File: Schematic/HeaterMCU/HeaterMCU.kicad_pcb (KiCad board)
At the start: 2 copper layers, 100 x 35 mm, 58 parts, among them J301 To µTracer, J302 Firmware, J303 To PSU Board, Q301 BSS138, Q302 BSS138, SW301 RESET, U301 TPS54302, U302 ATMEGA328P-AU, U303 INA219AIDCNR, U304 Display_IPS_1.3_SPI, Y301 8MHz

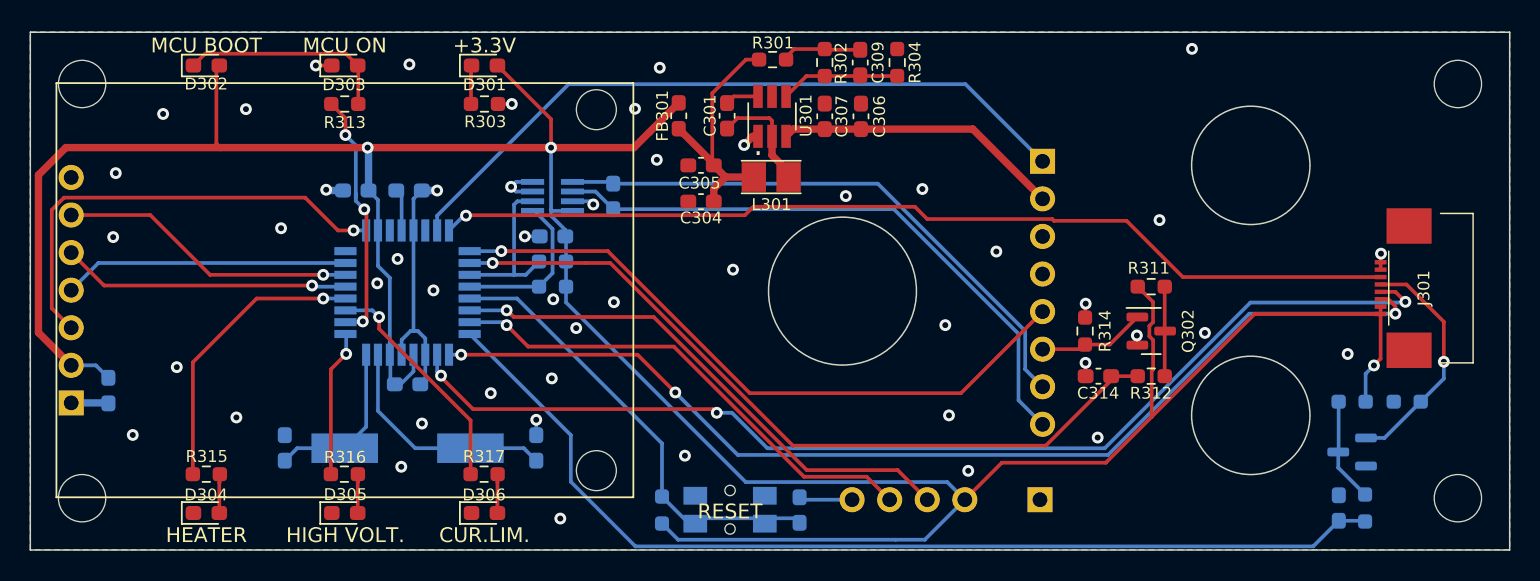
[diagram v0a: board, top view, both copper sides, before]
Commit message: Added output filter caps + spacing around mounting holes
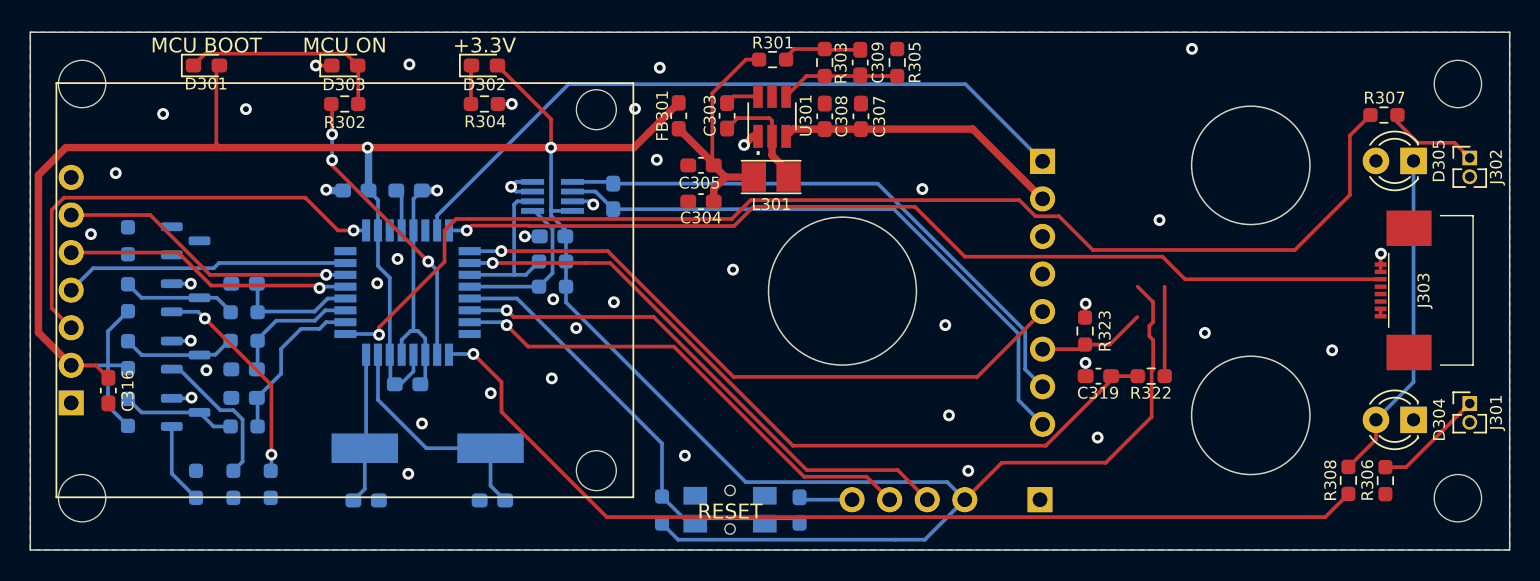
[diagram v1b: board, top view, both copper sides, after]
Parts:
- removed the D304 at (66.9, 77.5)
- added C313: 1µF, Capacitor_SMD:C_0603_1608Metric_Pad1.08x0.95mm_HandSolder, B.Cu at (69.5, 67.8)
- added C315: 1µF, Capacitor_SMD:C_0603_1608Metric_Pad1.08x0.95mm_HandSolder, B.Cu at (69.5, 62.0)
- added J301: Ext.LED, Connector_PinHeader_1.27mm:PinHeader_1x02_P1.27mm_Vertical, F.Cu at (152.3, 70.1)
- added J302: Ext.LED, Connector_PinHeader_1.27mm:PinHeader_1x02_P1.27mm_Vertical, F.Cu at (152.3, 53.5)
- added Q301: BSS138, Package_TO_SOT_SMD:SOT-23, B.Cu at (65.5, 66.8)
- added Q302: BSS138, Package_TO_SOT_SMD:SOT-23, B.Cu at (65.5, 63.0)
- added R312: 1MΩ, Resistor_SMD:R_0603_1608Metric_Pad0.98x0.95mm_HandSolder, B.Cu at (61.6, 66.8)
- added R313: 220Ω, Resistor_SMD:R_0603_1608Metric_Pad0.98x0.95mm_HandSolder, B.Cu at (69.5, 65.9)
- added R314: 100kΩ, Resistor_SMD:R_0603_1608Metric_Pad0.98x0.95mm_HandSolder, B.Cu at (68.7, 75.6)
- added R315: 1MΩ, Resistor_SMD:R_0603_1608Metric_Pad0.98x0.95mm_HandSolder, B.Cu at (61.6, 63.0)
- added R316: 220Ω, Resistor_SMD:R_0603_1608Metric_Pad0.98x0.95mm_HandSolder, B.Cu at (69.5, 63.9)
- added R317: 100kΩ, Resistor_SMD:R_0603_1608Metric_Pad0.98x0.95mm_HandSolder, B.Cu at (71.2, 75.6)
- C316: moved to F.Cu
- D304: renamed from D306; footprint LED_SMD:LED_0603_1608Metric_Pad1.05x0.95mm_HandSolder -> LED_THT:LED_D3.0mm
- D305: value "High Voltage" -> "Voltage limit"; footprint LED_SMD:LED_0603_1608Metric_Pad1.05x0.95mm_HandSolder -> LED_THT:LED_D3.0mm
- Q304: renamed from Q302; moved to B.Cu
- R306: renamed from R315; value 560Ω -> 330Ω
- R321: renamed from R311; moved to B.Cu
- moved R318 82.8 mm to (61.6, 70.7), turned to 90 degrees
- moved R320 82.1 mm to (66.2, 75.6), turned to 90 degrees
- moved R306 79.7 mm to (146.6, 75.3), turned to -90 degrees
- moved Q303 78.9 mm to (65.5, 70.7), turned to 0 degrees
- moved D305 76.1 mm to (148.5, 53.7), turned to 180 degrees
- moved R319 76.0 mm to (69.5, 71.7), turned to 180 degrees
- moved C318 74.4 mm to (69.5, 69.7), turned to 0 degrees
- moved R307 74.3 mm to (146.5, 50.6)
- moved R321 69.2 mm to (61.6, 59.1), turned to 90 degrees
- moved Q304 65.6 mm to (65.5, 59.1)
- moved D304 63.1 mm to (148.5, 71.2), turned to 180 degrees
- moved R308 58.4 mm to (144.1, 75.3), turned to -90 degrees
- moved C310 6.55 mm to (77.7, 76.7), turned to 0 degrees
- moved C306 4.62 mm to (86.2, 76.7), turned to 180 degrees
- moved Y301 1.36 mm to (81.9, 73.1)
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- renumbered C302 to C301, C303 to C302, C301 to C303, C308 to C306, C306 to C307, C307 to C308, C313 to C312, C315 to C314, C312 to C318, C314 to C319, D302 to D301, D301 to D302, J301 to J303, J302 to J304, J303 to J305, Q301 to Q303, R313 to R302, R302 to R303, R303 to R304, R304 to R305, R316 to R307, R317 to R308, R307 to R309, R308 to R310, R309 to R311, R305 to R318, R306 to R319, R310 to R320, R312 to R322, R314 to R323
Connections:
- net /FlagHeater renamed PULSE_HEATER
- net CUR_LIM renamed PULSE_CUR_LIM
- net FLAG_CUR_LIM_FILT renamed FLAG_CUR_LIM
- C318 pad 2: FLAG_HEATER_FILT -> FLAG_HEATER
- D304 pad 2: Net-(D306-Pad2) -> Net-(D304-Pad2)
- D305 pad 1: GNDPWR -> Net-(D304-Pad2)
- D305 pad 2: Net-(D305-Pad2) -> +3V3
- J303 pad 3: Spare2 -> PULSE_ANODE
- J303 pad 4: Spare1 -> PULSE_GRID
- R307 pad 1: Net-(D305-Pad2) -> Net-(J302-Pad1)
- R308 pad 1: Net-(D306-Pad2) -> Net-(D304-Pad2)
- R308 pad 2: LED_CURRENT_LIMIT -> LED_LIMIT_V_I
- R319 pad 1: FLAG_HEATER_FILT -> FLAG_HEATER
- U302 pad 1: Spare2 -> LED_LIMIT_V_I
- U302 pad 10: LED_MCU_STATUS -> FLAG_HEATER
- U302 pad 11: LED_CURRENT_LIMIT -> FLAG_ANODE
- U302 pad 12: LED_HEATER -> FLAG_GRID
- U302 pad 2: Spare1 -> LED_MCU_STATUS
- U302 pad 32: FLAG_HEATER_FILT -> LED_HEATER
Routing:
- net Spare1: track 74.9 -> 0.00 mm, vias 3 -> 0
- net LED_HIGH_VOLTAGE: track 9.62 -> 82.1 mm
- net Spare2: track 72.4 -> 0.00 mm, vias 3 -> 0
- net FLAG_HEATER_FILT: track 69.1 -> 0.00 mm
- net LED_LIMIT_V_I: track 0.00 -> 67.2 mm, vias 0 -> 1
- net Net-(D304-Pad2): track 0.00 -> 22.5 mm
- net LED_HEATER: track 19.4 -> 0.00 mm, vias 1 -> 0
- net LED_CURRENT_LIMIT: track 15.6 -> 0.00 mm, vias 1 -> 0
- net PULSE_GRID: track 0.00 -> 14.6 mm, vias 0 -> 2
- net +3V3: track 210.8 -> 198.9 mm, vias 3 -> 2
- net FLAG_HEATER: track 0.00 -> 11.0 mm
- net PULSE_HEATER: track 16.1 -> 5.50 mm, vias 1 -> 0
- net PULSE_ANODE: track 0.00 -> 9.93 mm
- net FLAG_ANODE: track 0.00 -> 8.66 mm
- net FLAG_GRID: track 0.00 -> 8.21 mm
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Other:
- board text added: "µTracer Heater MCU 22_43_0120F Bjørner Sandom"
- board text removed: "CUR.LIM."
- board text removed: "HEATER"
- board text removed: "HIGH VOLT."
- board text removed: "µTracer Heater MCU 22_43_0120E Bjørner Sandom"

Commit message: New status LED layout
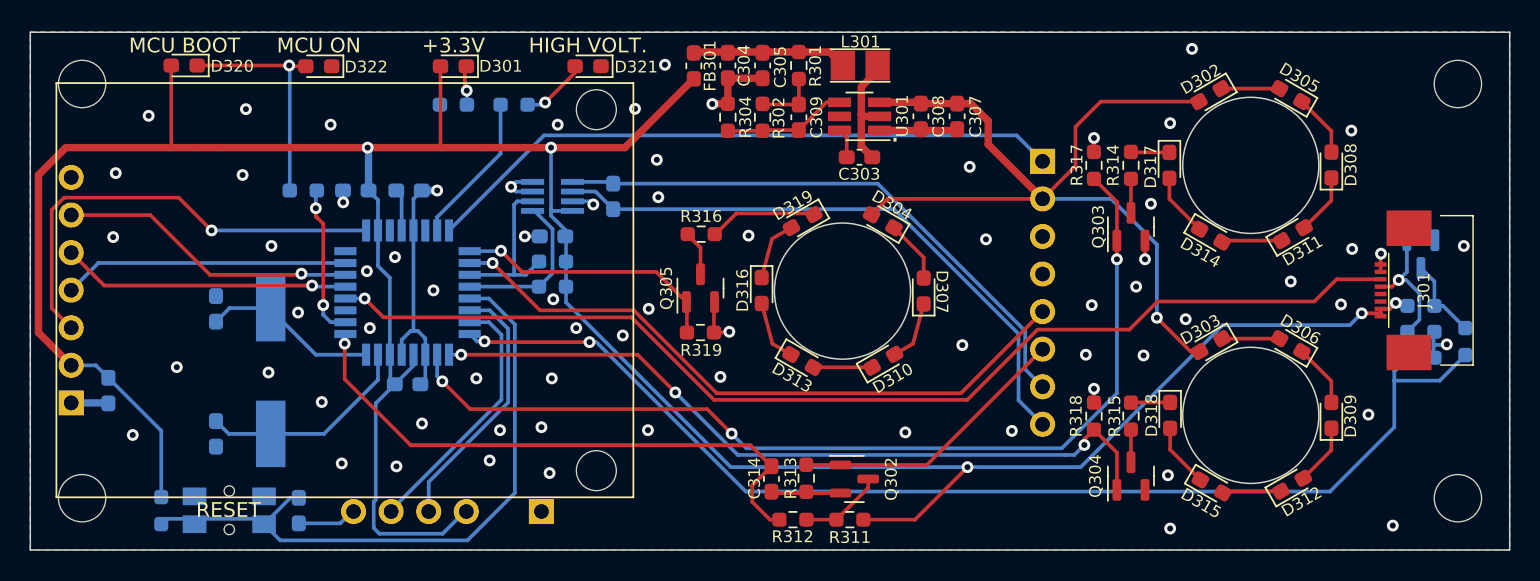
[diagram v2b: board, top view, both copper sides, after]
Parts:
- removed the C313 at (69.5, 67.8)
- removed the C315 at (69.5, 62.0)
- removed the J301 at (152.3, 70.1)
- removed the J302 at (152.3, 53.5)
- removed the Q301 at (65.5, 66.8)
- removed the Q302 at (65.5, 63.0)
- removed the R306 at (146.6, 75.3)
- removed the R307 at (146.5, 50.6)
- removed the R312 at (61.6, 66.8)
- removed the R313 at (69.5, 65.9)
- removed the R314 at (68.7, 75.6)
- added D303: "Current limit", LED_SMD:LED_0603_1608Metric_Pad1.05x0.95mm_HandSolder, F.Cu at (134.8, 66.2)
- added D305: "Voltage limit", LED_SMD:LED_0603_1608Metric_Pad1.05x0.95mm_HandSolder, F.Cu at (140.2, 49.2)
- added D306: "Current limit", LED_SMD:LED_0603_1608Metric_Pad1.05x0.95mm_HandSolder, F.Cu at (140.2, 66.2)
- added D307: "Heater", LED_SMD:LED_0603_1608Metric_Pad1.05x0.95mm_HandSolder, F.Cu at (115.4, 62.5)
- added D308: "Voltage limit", LED_SMD:LED_0603_1608Metric_Pad1.05x0.95mm_HandSolder, F.Cu at (142.9, 54.0)
- added D309: "Current limit", LED_SMD:LED_0603_1608Metric_Pad1.05x0.95mm_HandSolder, F.Cu at (142.9, 70.9)
- added D310: "Heater", LED_SMD:LED_0603_1608Metric_Pad1.05x0.95mm_HandSolder, F.Cu at (112.7, 67.2)
- added D311: "Voltage limit", LED_SMD:LED_0603_1608Metric_Pad1.05x0.95mm_HandSolder, F.Cu at (140.3, 58.6)
- added D312: "Current limit", LED_SMD:LED_0603_1608Metric_Pad1.05x0.95mm_HandSolder, F.Cu at (140.3, 75.6)
- added D313: "Heater", LED_SMD:LED_0603_1608Metric_Pad1.05x0.95mm_HandSolder, F.Cu at (107.2, 67.2)
- added D314: "Voltage limit", LED_SMD:LED_0603_1608Metric_Pad1.05x0.95mm_HandSolder, F.Cu at (134.8, 58.8)
- added D315: "Current limit", LED_SMD:LED_0603_1608Metric_Pad1.05x0.95mm_HandSolder, F.Cu at (134.8, 75.7)
- added D316: "Heater", LED_SMD:LED_0603_1608Metric_Pad1.05x0.95mm_HandSolder, F.Cu at (104.4, 62.5)
- added D317: "Voltage limit", LED_SMD:LED_0603_1608Metric_Pad1.05x0.95mm_HandSolder, F.Cu at (132.0, 54.0)
- added D318: "Current limit", LED_SMD:LED_0603_1608Metric_Pad1.05x0.95mm_HandSolder, F.Cu at (132.1, 70.9)
- added D319: "Heater", LED_SMD:LED_0603_1608Metric_Pad1.05x0.95mm_HandSolder, F.Cu at (107.2, 57.8)
- added D321: "HighVoltage", LED_SMD:LED_0603_1608Metric_Pad1.05x0.95mm_HandSolder, F.Cu at (92.7, 47.3)
- added Q303: BSS138, Package_TO_SOT_SMD:SOT-23, F.Cu at (129.4, 58.1)
- added Q304: BSS138, Package_TO_SOT_SMD:SOT-23, F.Cu at (129.4, 75.0)
- added Q305: BSS138, Package_TO_SOT_SMD:SOT-23, F.Cu at (100.3, 62.3)
- added R318: 100kΩ, Resistor_SMD:R_0603_1608Metric_Pad0.98x0.95mm_HandSolder, F.Cu at (126.9, 71.0)
- added R319: 100kΩ, Resistor_SMD:R_0603_1608Metric_Pad0.98x0.95mm_HandSolder, F.Cu at (100.3, 65.3)
- added R320: 560Ω, Resistor_SMD:R_0603_1608Metric_Pad0.98x0.95mm_HandSolder, B.Cu at (87.7, 49.9)
- C316: moved to B.Cu
- D302: renamed from D305; footprint LED_THT:LED_D3.0mm -> LED_SMD:LED_0603_1608Metric_Pad1.05x0.95mm_HandSolder
- D304: value "Current limit" -> "Heater"; footprint LED_THT:LED_D3.0mm -> LED_SMD:LED_0603_1608Metric_Pad1.05x0.95mm_HandSolder
- Q302: renamed from Q304; moved to F.Cu
- R303: renamed from R304; moved to B.Cu
- R311: renamed from R321; moved to F.Cu
- R314: renamed from R308; value 330Ω -> 2.7kΩ
- R315: value 1MΩ -> 2.7kΩ; moved to F.Cu
- R316: value 220Ω -> 2.7kΩ; moved to F.Cu
- R317: moved to F.Cu
- R321: renamed from R302; moved to B.Cu
- moved R305 87.7 mm to (149.0, 63.5), turned to 0 degrees
- moved Q301 84.2 mm to (149.0, 60.0), turned to -90 degrees
- moved R310 83.4 mm to (149.0, 65.2), turned to 0 degrees
- moved R306 82.7 mm to (152.0, 65.9), turned to 90 degrees
- moved C312 79.6 mm to (149.0, 67.0), turned to 180 degrees
- moved R315 68.3 mm to (129.4, 71.0), turned to -90 degrees
- moved R317 59.7 mm to (126.9, 54.0), turned to 90 degrees
- moved R311 52.3 mm to (110.4, 78.0), turned to 180 degrees
- moved Q302 48.0 mm to (110.7, 75.2)
- moved D304 38.3 mm to (112.6, 57.8), turned to 150 degrees
- moved G*** 34.8 mm to (110.2, 70.5)
- moved R307 33.9 mm to (63.9, 77.3), turned to -90 degrees
- moved C313 33.9 mm to (73.2, 77.3), turned to 90 degrees
- moved SW301 33.9 mm to (68.5, 77.5)
- moved J302 33.7 mm to (89.5, 77.4)
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- renumbered C318 to C312, C312 to C313, C319 to C314, C314 to C315, D302 to D301, D301 to D320, D303 to D322, J303 to J301, J304 to J302, J305 to J303, Q303 to Q301, R303 to R302, R305 to R304, R318 to R305, R319 to R306, R309 to R307, R310 to R308, R311 to R309, R320 to R310, R322 to R312, R323 to R313
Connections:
- net PULSE_CUR_LIM renamed CUR_LIM
- net PULSE_HEATER renamed /FlagHeater
- C312 pad 2: FLAG_HEATER -> FLAG_HEATER_FILT
- C314 pad 2: FLAG_CUR_LIM -> FLAG_CUR_LIM_FILT
- D302 pad 1: Net-(D304-Pad2) -> Net-(D302-Pad1)
- D302 pad 2: +3V3 -> VDC
- D304 pad 1: GNDPWR -> Net-(D304-Pad1)
- D304 pad 2: Net-(D304-Pad2) -> VDC
- J301 pad 3: PULSE_ANODE -> unconnected-(J301-Pad3)
- J301 pad 4: PULSE_GRID -> unconnected-(J301-Pad4)
- R306 pad 1: FLAG_HEATER -> FLAG_HEATER_FILT
- R312 pad 1: FLAG_CUR_LIM -> FLAG_CUR_LIM_FILT
- R314 pad 1: Net-(D304-Pad2) -> Net-(D317-Pad1)
- R314 pad 2: LED_LIMIT_V_I -> Net-(R314-Pad2)
- R315 pad 1: +3V3 -> Net-(D318-Pad1)
- R315 pad 2: Net-(Q302-Pad3) (its old number) -> Net-(Q304-Pad3)
- R316 pad 1: FLAG_GRID -> Net-(D319-Pad1)
- R316 pad 2: Net-(Q302-Pad3) (its old number) -> Net-(Q305-Pad3)
- R317 pad 1: PULSE_GRID -> LED_LIMIT_V
- U302 pad 1: LED_LIMIT_V_I -> LED_LIMIT_I
- U302 pad 10: FLAG_HEATER -> LED_MCU_STATUS
- U302 pad 11: FLAG_ANODE -> unconnected-(U302-Pad11)
- U302 pad 12: FLAG_GRID -> FLAG_HIGH_VOLTAGE
- U302 pad 2: LED_MCU_STATUS -> LED_LIMIT_V
- U302 pad 23: PSU_EN -> LED_HIGH_VOLTAGE
- U302 pad 24: FLAG_HIGH_VOLTAGE -> PSU_EN
- U302 pad 25: OUT_EN -> LED_HEATER
- U302 pad 26: FLAG_CUR_LIM -> OUT_EN
- U302 pad 32: LED_HEATER -> FLAG_HEATER_FILT
- U302 pad 9: LED_HIGH_VOLTAGE -> FLAG_CUR_LIM_FILT
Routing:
- net FLAG_HEATER_FILT: track 0.00 -> 79.3 mm, vias 0 -> 2
- net LED_HIGH_VOLTAGE: track 82.1 -> 10.3 mm, vias 1 -> 0
- net LED_LIMIT_V_I: track 67.2 -> 0.00 mm, vias 1 -> 0
- net LED_LIMIT_V: track 0.00 -> 66.1 mm, vias 0 -> 3
- net FLAG_CUR_LIM: track 52.4 -> 0.00 mm, vias 1 -> 0
- net LED_LIMIT_I: track 0.00 -> 52.1 mm, vias 0 -> 3
- net VDC: track 19.5 -> 59.3 mm, vias 0 -> 1
- net FLAG_CUR_LIM_FILT: track 0.00 -> 39.6 mm, vias 0 -> 1
- net Net-(D304-Pad2): track 22.5 -> 0.00 mm
- net Net-(J302-Pad4): track 36.2 -> 17.6 mm, vias 1 -> 0
- net LED_HEATER: track 0.00 -> 18.2 mm, vias 0 -> 1
- net GNDPWR: track 34.0 -> 51.3 mm, vias 43 -> 71
- net Net-(J302-Pad5): track 33.4 -> 17.4 mm, vias 1 -> 0
- net PULSE_GRID: track 14.6 -> 0.00 mm, vias 2 -> 0
- net Net-(C313-Pad2): track 31.0 -> 44.2 mm
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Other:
- outline, holes or cut-outs redrawn
- board text added: "HIGH VOLT."
